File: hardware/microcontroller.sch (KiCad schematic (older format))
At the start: 14 parts, among them J4 Conn_02x05_Odd_Even, U11 STM32G431CBT6

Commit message: Layout almost complete. Just needs a tidy.
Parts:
- removed J4: Conn_02x05_Odd_Even, Connector_PinHeader_2.54mm:PinHeader_2x05_P2.54mm_Vertical, symbol Connector_Generic:Conn_02x05_Odd_Even
- added J4: Conn_02x05_Counter_Clockwise, Connector:Tag-Connect_TC2050-IDC-NL_2x05_P1.27mm_Vertical, symbol Connector_Generic:Conn_02x05_Counter_Clockwise
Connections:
- net +3V3_STBY: now also J4.1 (Pin_1)
- net CHA_CUR: now also U11.12 (PA4); no longer U11.9 (PA1)
- net CHA_TEMP: now also U11.13 (PA5); no longer U11.10 (PA2)
- net CHA_VOL: now also U11.11 (PA3); no longer U11.8 (PA0)
- net CHB_CUR: now also U11.9 (PA1); no longer U11.12 (PA4)
- net CHB_TEMP: now also U11.10 (PA2); no longer U11.13 (PA5)
- net CHB_VOL: now also U11.8 (PA0); no longer U11.11 (PA3)
- net GND: now also J4.3 (Pin_3), J4.5 (Pin_5)
- net TCK: now also J4.4 (Pin_4)
- net TDI: now also J4.8 (Pin_8)
- net TDO: now also J4.6 (Pin_6)
- net TMS: now also J4.2 (Pin_2)
- net ~RST: now also J4.10 (Pin_10)
- net EN_12V: now reaches U11.5 (PF0-OSC_IN)
- net EN_3V3: now reaches U11.6 (PF1-OSC_OUT)
- net TRST renamed ~TRST
- net ~TRST: now also J4.9 (Pin_9)
- no-connect marks 13 -> 11
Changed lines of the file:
@@
 Text HLabel 5650 2450 0    50   Output ~ 0
 CHA_LO
-Text HLabel 5650 1350 0    50   Input ~ 0
+Text HLabel 5650 1650 0    50   Input ~ 0
 CHA_VOL
-Text HLabel 5650 1450 0    50   Input ~ 0
+Text HLabel 5650 1750 0    50   Input ~ 0
 CHA_CUR
-Text HLabel 5650 1550 0    50   Input ~ 0
+Text HLabel 5650 1850 0    50   Input ~ 0
 CHA_TEMP
 Text HLabel 5650 2250 0    50   Output ~ 0
@@
 Text HLabel 5650 2550 0    50   Output ~ 0
 CHB_LO
-Text HLabel 5650 1650 0    50   Input ~ 0
+Text HLabel 5650 1350 0    50   Input ~ 0
 CHB_VOL
-Text HLabel 5650 1750 0    50   Input ~ 0
+Text HLabel 5650 1450 0    50   Input ~ 0
 CHB_CUR
-Text HLabel 5650 1850 0    50   Input ~ 0
+Text HLabel 5650 1550 0    50   Input ~ 0
 CHB_TEMP
 $Comp
@@
 	5650 2250 5750 2250
 Wire Wire Line
+	5650 1650 5750 1650
+Wire Wire Line
+	5650 1750 5750 1750
+Wire Wire Line
+	5750 2450 5650 2450
+Wire Wire Line
+	5750 2550 5650 2550
+Wire Wire Line
 	5650 1350 5750 1350
 Wire Wire Line
 	5650 1450 5750 1450
 Wire Wire Line
-	5750 2450 5650 2450
-Wire Wire Line
-	5750 2550 5650 2550
-Wire Wire Line
-	5650 1650 5750 1650
-Wire Wire Line
-	5650 1750 5750 1750
+	5650 1850 5750 1850
 Wire Wire Line
 	5650 1550 5750 1550
-Wire Wire Line
-	5650 1850 5750 1850
 Wire Wire Line
 	8200 2750 8300 2750
@@
 	9100 2300 9100 2250
 Text Label 8700 1750 2    50   ~ 0
-TRST
+~TRST
 Text Label 8700 1650 2    50   ~ 0
 TDO
@@
 NoConn ~ 8200 2350
 NoConn ~ 8200 2450
-NoConn ~ 8200 3050
-NoConn ~ 8200 3150
 NoConn ~ 5750 3150
 NoConn ~ 5750 3250
@@
 NoConn ~ 5750 1950
 $Comp
-L Connector_Generic:Conn_02x05_Odd_Even J4
-U 1 1 5F5A8B34
-P 6850 5100
-F 0 "J4" H 6900 5425 50  0000 C CNN
-F 1 "Conn_02x05_Odd_Even" H 6900 5426 50  0001 C CNN
-F 2 "Connector_PinHeader_2.54mm:PinHeader_2x05_P2.54mm_Vertical" H 6850 5100 50  0001 C CNN
-F 3 "~" H 6850 5100 50  0001 C CNN
-	1    6850 5100
-	1    0    0    -1
-$EndComp
-$Comp
 L Station:+3V3_STBY #PWR045
 U 1 1 5F5AB1B9
-P 6500 4750
-F 0 "#PWR045" H 6500 4600 50  0001 C CNN
-F 1 "+3V3_STBY" H 6515 4923 50  0000 C CNN
-F 2 "" H 6500 4750 50  0001 C CNN
-F 3 "" H 6500 4750 50  0001 C CNN
-	1    6500 4750
+P 6300 4700
+F 0 "#PWR045" H 6300 4550 50  0001 C CNN
+F 1 "+3V3_STBY" H 6315 4873 50  0000 C CNN
+F 2 "" H 6300 4700 50  0001 C CNN
+F 3 "" H 6300 4700 50  0001 C CNN
+	1    6300 4700
 	1    0    0    -1
 $EndComp
@@
 $EndComp
 Wire Wire Line
-	6500 4750 6500 4900
-Wire Wire Line
-	6500 4900 6650 4900
-Wire Wire Line
-	6650 5000 6500 5000
-Wire Wire Line
-	6500 5000 6500 5100
-Wire Wire Line
-	6500 5100 6650 5100
-Wire Wire Line
-	6500 5100 6500 5300
-Wire Wire Line
-	6500 5300 6650 5300
-Connection ~ 6500 5100
-NoConn ~ 6650 5200
+	6300 4700 6300 4850
+Wire Wire Line
+	6300 4850 6650 4850
+Wire Wire Line
+	6300 5250 6650 5250
 $Comp
 L power:GND #PWR046
 U 1 1 5F5BC388
-P 6500 5400
-F 0 "#PWR046" H 6500 5150 50  0001 C CNN
-F 1 "GND" H 6505 5227 50  0000 C CNN
-F 2 "" H 6500 5400 50  0001 C CNN
-F 3 "" H 6500 5400 50  0001 C CNN
-	1    6500 5400
-	1    0    0    -1
-$EndComp
-Wire Wire Line
-	6500 5300 6500 5400
-Connection ~ 6500 5300
-Wire Wire Line
-	7150 4900 7400 4900
-Wire Wire Line
-	7150 5000 7400 5000
-Wire Wire Line
-	7150 5100 7400 5100
-Wire Wire Line
-	7150 5200 7400 5200
-Wire Wire Line
-	7150 5300 7400 5300
-Text Label 7400 4900 2    50   ~ 0
+P 6300 5400
+F 0 "#PWR046" H 6300 5150 50  0001 C CNN
+F 1 "GND" H 6305 5227 50  0000 C CNN
+F 2 "" H 6300 5400 50  0001 C CNN
+F 3 "" H 6300 5400 50  0001 C CNN
+	1    6300 5400
+	1    0    0    -1
+$EndComp
+Wire Wire Line
+	6300 5250 6300 5400
+Wire Wire Line
+	6650 4950 6400 4950
+Wire Wire Line
+	6650 5150 6400 5150
+Text Label 6400 4950 0    50   ~ 0
 TMS
-Text Label 7400 5000 2    50   ~ 0
+Text Label 6400 5150 0    50   ~ 0
 TCK
-Text Label 7400 5100 2    50   ~ 0
-TDO
-Text Label 7400 5200 2    50   ~ 0
-TDI
-Text Label 7400 5300 2    50   ~ 0
-~RST
 $Comp
 L Station:+3V3_STBY #PWR048
@@
 Wire Wire Line
 	5650 2050 5750 2050
+$Comp
+L Connector_Generic:Conn_02x05_Counter_Clockwise J4
+U 1 1 607C3506
+P 6850 5050
+F 0 "J4" H 6900 5375 50  0000 C CNN
+F 1 "Conn_02x05_Counter_Clockwise" H 6900 5376 50  0001 C CNN
+F 2 "Connector:Tag-Connect_TC2050-IDC-NL_2x05_P1.27mm_Vertical" H 6850 5050 50  0001 C CNN
+F 3 "~" H 6850 5050 50  0001 C CNN
+	1    6850 5050
+	1    0    0    -1
+$EndComp
+NoConn ~ 7150 5150
+Wire Wire Line
+	7150 4950 7400 4950
+Wire Wire Line
+	6300 5050 6300 5250
+Wire Wire Line
+	6300 5050 6650 5050
+Connection ~ 6300 5250
+Text Label 7400 5250 2    50   ~ 0
+TDO
+Wire Wire Line
+	7150 5250 7400 5250
+Text Label 7400 5050 2    50   ~ 0
+TDI
+Wire Wire Line
+	7150 5050 7400 5050
+Text Label 7400 4850 2    50   ~ 0
+~RST
+Wire Wire Line
+	7150 4850 7400 4850
+Text Label 7400 4950 2    50   ~ 0
+~TRST
+Text HLabel 8300 3050 2    50   Output ~ 0
+EN_12V
+Wire Wire Line
+	8200 3050 8300 3050
+Text HLabel 8300 3150 2    50   Output ~ 0
+EN_3V3
+Wire Wire Line
+	8200 3150 8300 3150
 $EndSCHEMATC

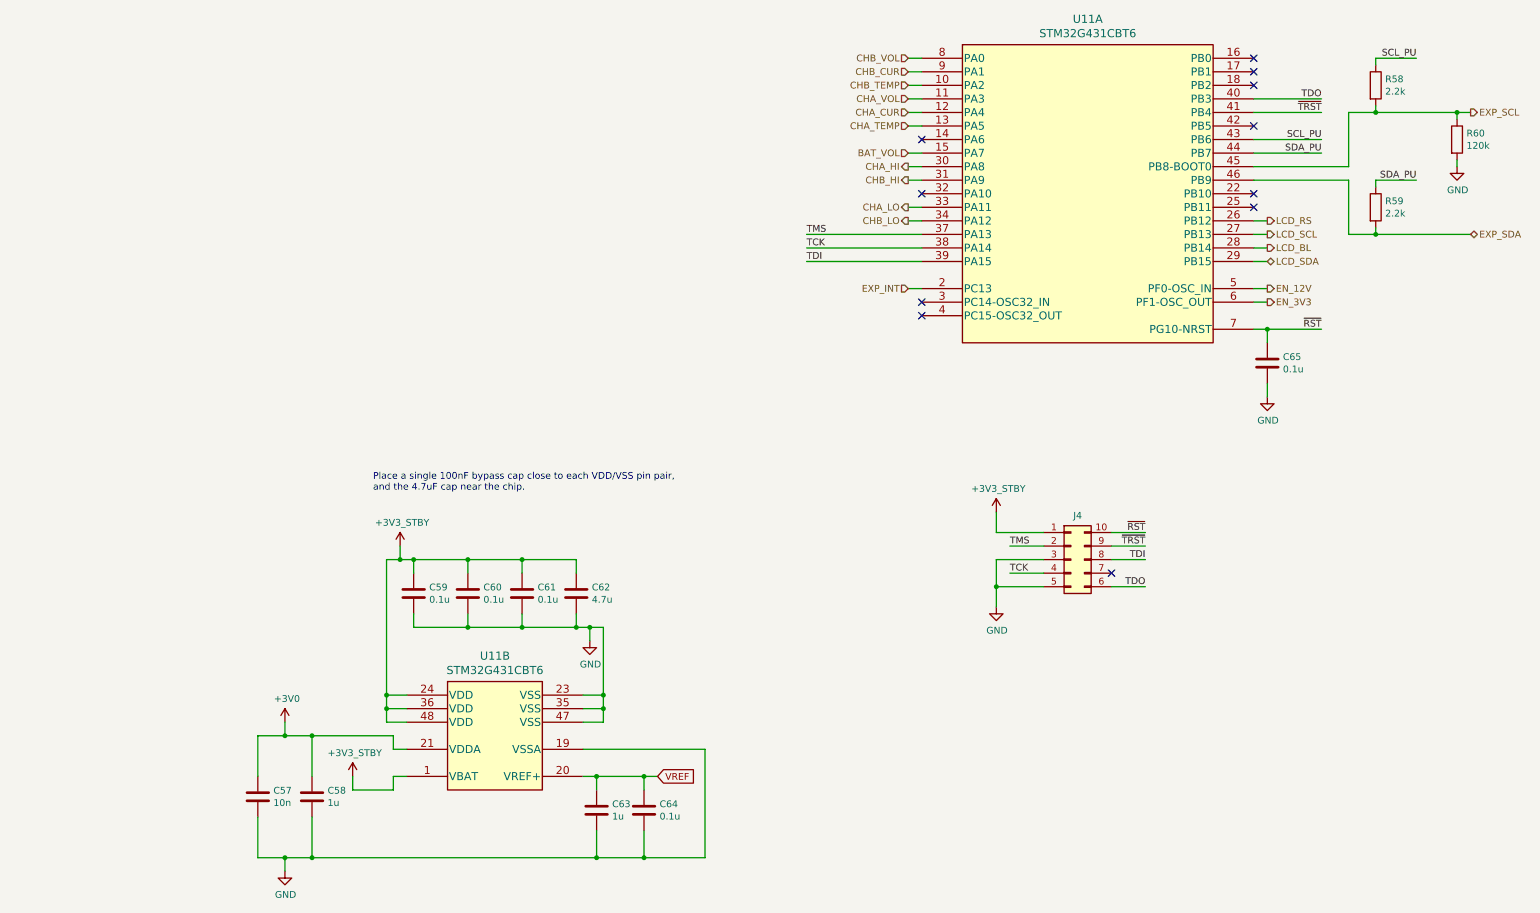
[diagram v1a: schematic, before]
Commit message: Update BOM * Datasheets * Manufacturers * Part numbers
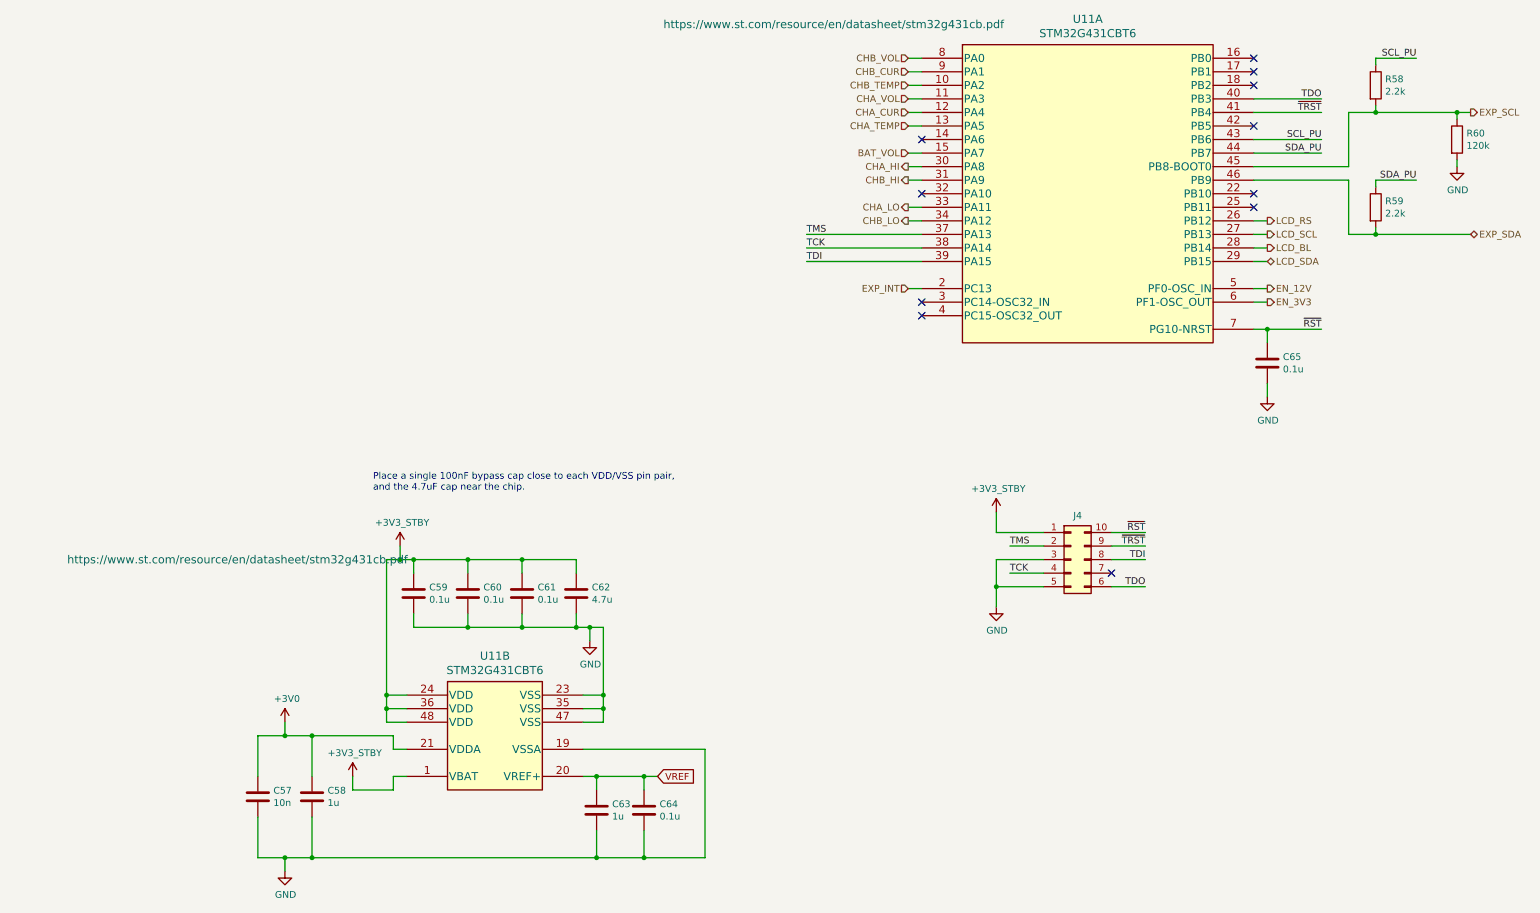
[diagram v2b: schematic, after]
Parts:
- C57: Manufacturer (none) -> TDK; Part Number (none) -> C1608X7R2A103K080AA; Tolerance (none) -> 10%; Voltage Rating 35 V -> 100 V
- C58, C63: Manufacturer (none) -> KEMET; Part Number (none) -> C1206C105K3RACAUTO; Tolerance (none) -> 10%
- C59, C60, C61, C64, C65: Manufacturer (none) -> Taiyo Yuden; Part Number (none) -> GMK107B7104KAHT; Tolerance (none) -> 10%
- C62: Manufacturer (none) -> Samsung; Part Number (none) -> CL31B475KAHNFNE; Tolerance (none) -> 10%; Voltage Rating (none) -> 25 V
- J4: DNP (none) -> X
- R58, R59: Manufacturer (none) -> Stackpole Electronics Inc; Part Number (none) -> RMCF0603JT2K20; Tolerance (none) -> 5%
- R60: Manufacturer (none) -> Stackpole Electronics Inc; Part Number (none) -> RMCF0603FT120K; Tolerance (none) -> 1%
- U11: Manufacturer (none) -> ST Microelectronics; Part Number (none) -> STM32G431CBT6
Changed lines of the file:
@@
 F 1 "1u" H 1365 6755 50  0000 L CNN
 F 2 "Capacitor_SMD:C_1206_3216Metric" H 1288 6650 50  0001 C CNN
-F 3 "~" H 1250 6800 50  0001 C CNN
+F 3 "https://api.kemet.com/component-edge/download/datasheet/C1206C105K3RACAUTO.pdf" H 1250 6800 50  0001 C CNN
 F 4 "25 V" H 1250 6800 50  0001 C CNN "Voltage Rating"
+F 5 "KEMET" H 1250 6800 50  0001 C CNN "Manufacturer"
+F 6 "C1206C105K3RACAUTO" H 1250 6800 50  0001 C CNN "Part Number"
+F 7 "10%" H 1250 6800 50  0001 C CNN "Tolerance"
 	1    1250 6800
 	1    0    0    -1
@@
 F 1 "0.1u" H 2115 5255 50  0000 L CNN
 F 2 "Capacitor_SMD:C_0603_1608Metric" H 2038 5150 50  0001 C CNN
-F 3 "~" H 2000 5300 50  0001 C CNN
+F 3 "https://ds.yuden.co.jp/TYCOMPAS/ut/detail?pn=GMK107B7104KAHT%20%20&u=M" H 2000 5300 50  0001 C CNN
 F 4 "35 V" H 2000 5300 50  0001 C CNN "Voltage Rating"
+F 5 "Taiyo Yuden" H 2000 5300 50  0001 C CNN "Manufacturer"
+F 6 "GMK107B7104KAHT" H 2000 5300 50  0001 C CNN "Part Number"
+F 7 "10%" H 2000 5300 50  0001 C CNN "Tolerance"
 	1    2000 5300
 	1    0    0    -1
@@
 F 1 "0.1u" H 2515 5255 50  0000 L CNN
 F 2 "Capacitor_SMD:C_0603_1608Metric" H 2438 5150 50  0001 C CNN
-F 3 "~" H 2400 5300 50  0001 C CNN
+F 3 "https://ds.yuden.co.jp/TYCOMPAS/ut/detail?pn=GMK107B7104KAHT%20%20&u=M" H 2400 5300 50  0001 C CNN
 F 4 "35 V" H 2400 5300 50  0001 C CNN "Voltage Rating"
+F 5 "Taiyo Yuden" H 2400 5300 50  0001 C CNN "Manufacturer"
+F 6 "GMK107B7104KAHT" H 2400 5300 50  0001 C CNN "Part Number"
+F 7 "10%" H 2400 5300 50  0001 C CNN "Tolerance"
 	1    2400 5300
 	1    0    0    -1
@@
 F 1 "0.1u" H 2915 5255 50  0000 L CNN
 F 2 "Capacitor_SMD:C_0603_1608Metric" H 2838 5150 50  0001 C CNN
-F 3 "~" H 2800 5300 50  0001 C CNN
+F 3 "https://ds.yuden.co.jp/TYCOMPAS/ut/detail?pn=GMK107B7104KAHT%20%20&u=M" H 2800 5300 50  0001 C CNN
 F 4 "35 V" H 2800 5300 50  0001 C CNN "Voltage Rating"
+F 5 "Taiyo Yuden" H 2800 5300 50  0001 C CNN "Manufacturer"
+F 6 "GMK107B7104KAHT" H 2800 5300 50  0001 C CNN "Part Number"
+F 7 "10%" H 2800 5300 50  0001 C CNN "Tolerance"
 	1    2800 5300
 	1    0    0    -1
@@
 F 1 "1u" H 3465 6855 50  0000 L CNN
 F 2 "Capacitor_SMD:C_1206_3216Metric" H 3388 6750 50  0001 C CNN
-F 3 "~" H 3350 6900 50  0001 C CNN
+F 3 "https://api.kemet.com/component-edge/download/datasheet/C1206C105K3RACAUTO.pdf" H 3350 6900 50  0001 C CNN
 F 4 "25 V" H 3350 6900 50  0001 C CNN "Voltage Rating"
+F 5 "KEMET" H 3350 6900 50  0001 C CNN "Manufacturer"
+F 6 "C1206C105K3RACAUTO" H 3350 6900 50  0001 C CNN "Part Number"
+F 7 "10%" H 3350 6900 50  0001 C CNN "Tolerance"
 	1    3350 6900
 	1    0    0    -1
@@
 F 1 "STM32G431CBT6" H 2600 6733 60  0000 C CNN
 F 2 "Package_QFP:LQFP-48_7x7mm_P0.5mm" H 2600 7500 60  0001 C CNN
-F 3 "" H 700 7550 60  0000 C CNN
+F 3 "https://www.st.com/resource/en/datasheet/stm32g431cb.pdf" H 700 7550 60  0000 C CNN
+F 4 "ST Microelectronics" H 2600 6300 50  0001 C CNN "Manufacturer"
+F 5 "STM32G431CBT6" H 2600 6300 50  0001 C CNN "Part Number"
 	2    2600 6300
 	1    0    0    -1
@@
 F 1 "10n" H 965 6755 50  0000 L CNN
 F 2 "Capacitor_SMD:C_0603_1608Metric" H 888 6650 50  0001 C CNN
-F 3 "~" H 850 6800 50  0001 C CNN
-F 4 "35 V" H 850 6800 50  0001 C CNN "Voltage Rating"
+F 3 "https://product.tdk.com/info/en/catalog/datasheets/mlcc_commercial_midvoltage_en.pdf?ref_disty=digikey" H 850 6800 50  0001 C CNN
+F 4 "100 V" H 850 6800 50  0001 C CNN "Voltage Rating"
+F 5 "TDK" H 850 6800 50  0001 C CNN "Manufacturer"
+F 6 "C1608X7R2A103K080AA" H 850 6800 50  0001 C CNN "Part Number"
+F 7 "10%" H 850 6800 50  0001 C CNN "Tolerance"
 	1    850  6800
 	1    0    0    -1
@@
 F 1 "0.1u" H 3815 6855 50  0000 L CNN
 F 2 "Capacitor_SMD:C_0603_1608Metric" H 3738 6750 50  0001 C CNN
-F 3 "~" H 3700 6900 50  0001 C CNN
+F 3 "https://ds.yuden.co.jp/TYCOMPAS/ut/detail?pn=GMK107B7104KAHT%20%20&u=M" H 3700 6900 50  0001 C CNN
 F 4 "35 V" H 3700 6900 50  0001 C CNN "Voltage Rating"
+F 5 "Taiyo Yuden" H 3700 6900 50  0001 C CNN "Manufacturer"
+F 6 "GMK107B7104KAHT" H 3700 6900 50  0001 C CNN "Part Number"
+F 7 "10%" H 3700 6900 50  0001 C CNN "Tolerance"
 	1    3700 6900
 	1    0    0    -1
@@
 F 1 "4.7u" H 3315 5255 50  0000 L CNN
 F 2 "Capacitor_SMD:C_1206_3216Metric" H 3238 5150 50  0001 C CNN
-F 3 "~" H 3200 5300 50  0001 C CNN
-F 4 "" H 3200 5300 50  0001 C CNN "Voltage Rating"
+F 3 "http://www.samsungsem.com/kr/support/product-search/mlcc/CL31B475KAHNFNE.jsp" H 3200 5300 50  0001 C CNN
+F 4 "25 V" H 3200 5300 50  0001 C CNN "Voltage Rating"
+F 5 "Samsung" H 3200 5300 50  0001 C CNN "Manufacturer"
+F 6 "CL31B475KAHNFNE" H 3200 5300 50  0001 C CNN "Part Number"
+F 7 "10%" H 3200 5300 50  0001 C CNN "Tolerance"
 	1    3200 5300
 	1    0    0    -1
@@
 F 1 "STM32G431CBT6" H 6975 3533 60  0000 C CNN
 F 2 "Package_QFP:LQFP-48_7x7mm_P0.5mm" H 7000 3550 60  0001 C CNN
-F 3 "" H 5100 3600 60  0000 C CNN
+F 3 "https://www.st.com/resource/en/datasheet/stm32g431cb.pdf" H 5100 3600 60  0000 C CNN
+F 4 "ST Microelectronics" H 7000 2350 50  0001 C CNN "Manufacturer"
+F 5 "STM32G431CBT6" H 7000 2350 50  0001 C CNN "Part Number"
 	1    7000 2350
 	1    0    0    -1
@@
 F 1 "120k" H 9770 1905 50  0000 L CNN
 F 2 "Resistor_SMD:R_0603_1608Metric" V 9630 1950 50  0001 C CNN
-F 3 "~" H 9700 1950 50  0001 C CNN
+F 3 "https://www.seielect.com/catalog/sei-packaging.pdf" H 9700 1950 50  0001 C CNN
+F 4 "Stackpole Electronics Inc" H 9700 1950 50  0001 C CNN "Manufacturer"
+F 5 "RMCF0603FT120K" H 9700 1950 50  0001 C CNN "Part Number"
+F 6 "1%" H 9700 1950 50  0001 C CNN "Tolerance"
 	1    9700 1950
 	1    0    0    -1
@@
 F 1 "2.2k" H 9170 1505 50  0000 L CNN
 F 2 "Resistor_SMD:R_0603_1608Metric" V 9030 1550 50  0001 C CNN
-F 3 "~" H 9100 1550 50  0001 C CNN
+F 3 "https://www.seielect.com/catalog/sei-rmcf_rmcp.pdf" H 9100 1550 50  0001 C CNN
+F 4 "Stackpole Electronics Inc" H 9100 1550 50  0001 C CNN "Manufacturer"
+F 5 "RMCF0603JT2K20" H 9100 1550 50  0001 C CNN "Part Number"
+F 6 "5%" H 9100 1550 50  0001 C CNN "Tolerance"
 	1    9100 1550
 	1    0    0    -1
@@
 F 1 "2.2k" H 9170 2405 50  0000 L CNN
 F 2 "Resistor_SMD:R_0603_1608Metric" V 9030 2450 50  0001 C CNN
-F 3 "~" H 9100 2450 50  0001 C CNN
+F 3 "https://www.seielect.com/catalog/sei-rmcf_rmcp.pdf" H 9100 2450 50  0001 C CNN
+F 4 "Stackpole Electronics Inc" H 9100 2450 50  0001 C CNN "Manufacturer"
+F 5 "RMCF0603JT2K20" H 9100 2450 50  0001 C CNN "Part Number"
+F 6 "5%" H 9100 2450 50  0001 C CNN "Tolerance"
 	1    9100 2450
 	1    0    0    -1
@@
 F 1 "0.1u" H 8415 3555 50  0000 L CNN
 F 2 "Capacitor_SMD:C_0603_1608Metric" H 8338 3450 50  0001 C CNN
-F 3 "~" H 8300 3600 50  0001 C CNN
+F 3 "https://ds.yuden.co.jp/TYCOMPAS/ut/detail?pn=GMK107B7104KAHT%20%20&u=M" H 8300 3600 50  0001 C CNN
 F 4 "35 V" H 8300 3600 50  0001 C CNN "Voltage Rating"
+F 5 "Taiyo Yuden" H 8300 3600 50  0001 C CNN "Manufacturer"
+F 6 "GMK107B7104KAHT" H 8300 3600 50  0001 C CNN "Part Number"
+F 7 "10%" H 8300 3600 50  0001 C CNN "Tolerance"
 	1    8300 3600
 	1    0    0    -1
@@
 F 2 "Connector:Tag-Connect_TC2050-IDC-NL_2x05_P1.27mm_Vertical" H 6850 5050 50  0001 C CNN
 F 3 "~" H 6850 5050 50  0001 C CNN
+F 4 "X" H 6850 5050 50  0001 C CNN "DNP"
 	1    6850 5050
 	1    0    0    -1
